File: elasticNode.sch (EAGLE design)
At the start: 101 parts, among them J1 ISP_CONN_6PIN, J2 FEMALE_HEADER_2X2, J3 FEMALE_HEADER_2X1, J4 FEMALE_HEADER_2X1, J5 FEMALE_HEADER_5X2, J6 FEMALE_HEADER_5X2, J7 JTAG_CONN_6PINTHT, J8 USB_CONNSMT, U1 ATMEGA64AQFN, U10 LTC3419DFN, U2 SST26VF032B, U3 MRF24J40MA, U4 SPARTAN6-LX9, U5 SST26VF032B, U6 PAC1720, U7 PAC1720, U8 PAC1720, U9 FT232RSSOP28, X1 12MHz, X2 50MHz, X3 32MHz

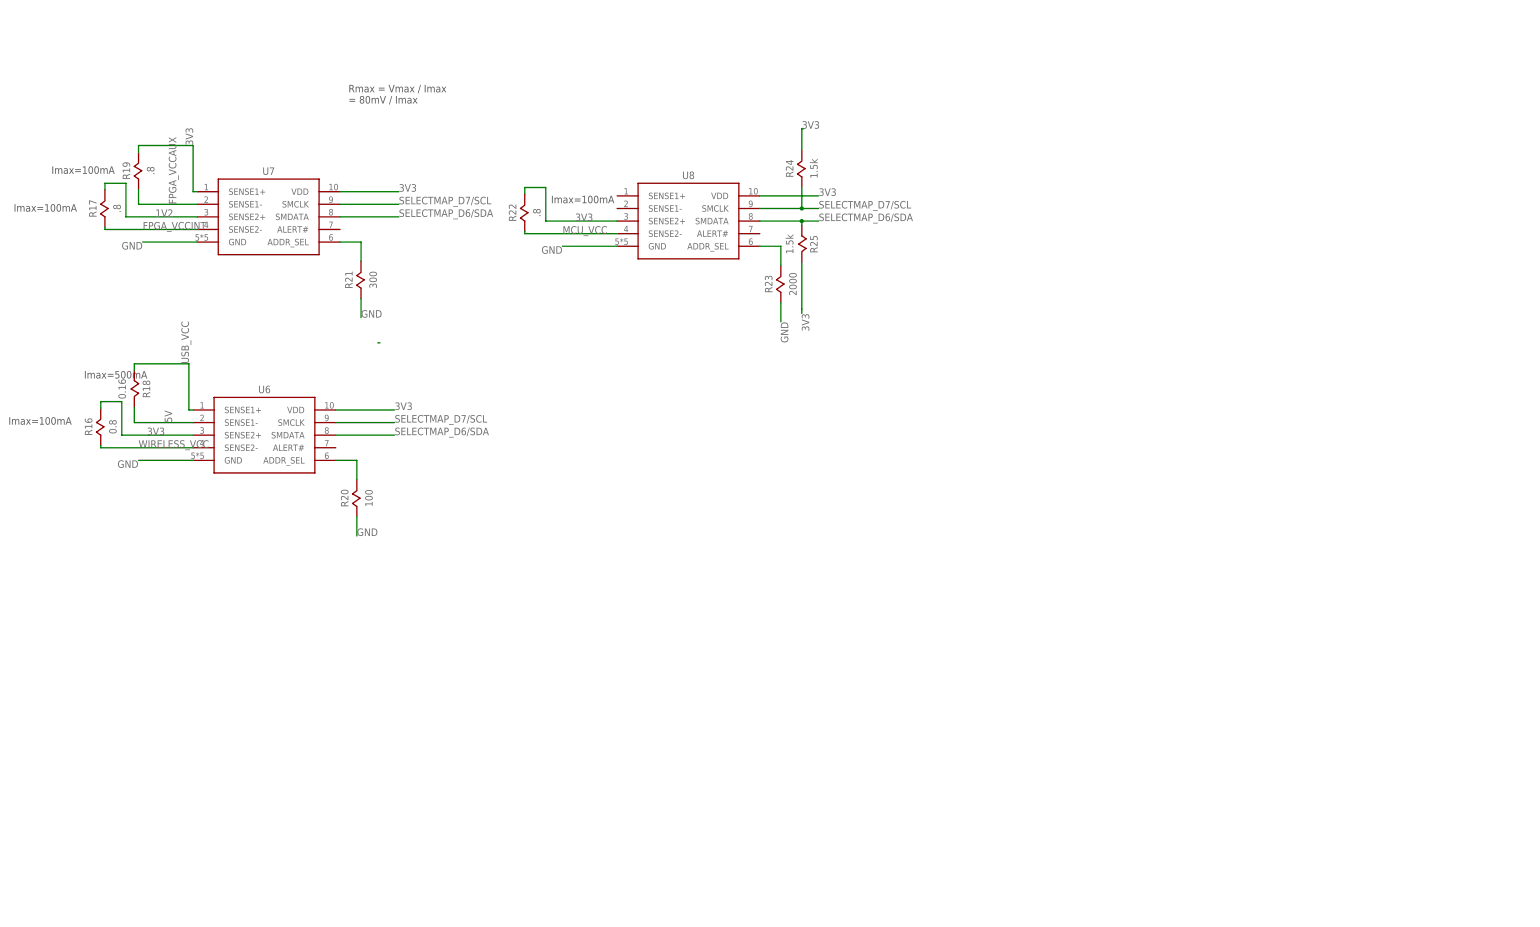
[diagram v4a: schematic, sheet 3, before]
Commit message: first part toward separate monitoring board
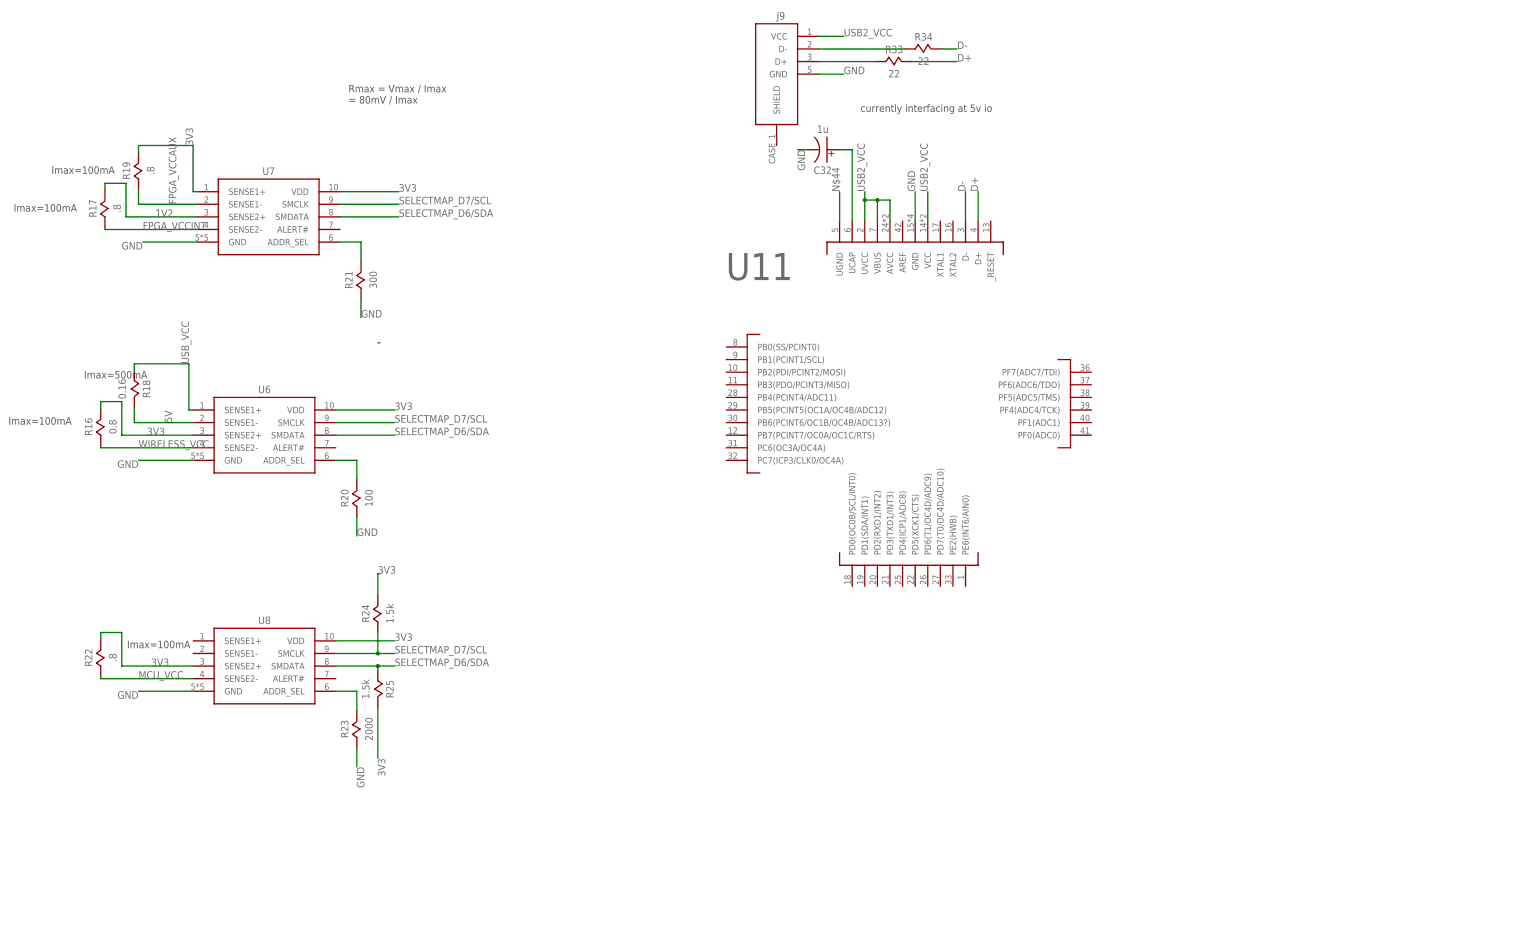
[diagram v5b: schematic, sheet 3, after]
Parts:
- added C32: 1u, passive:CAPACITOR0805
- added J9: USB_CONNSMT, connectors:USB_CONNSMT
- added R33, R34: 22, passive:RESISTOR
- added U11: ATMEGA32U4, ic:ATMEGA32U4
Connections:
- new net D+: R33.2, U11.D+
- new net D-: R34.2, U11.D-
- new net N$38: J9.D+, R33.1
- new net N$39: J9.D-, R34.1
- new net N$43: C32.P$1, U11.UCAP
- new net N$44: U11.UGND
- new net USB2_VCC: J9.VCC, U11.AVCC, U11.UVCC, U11.VBUS, U11.VCC
- net GND: now also C32.P$2, J9.GND, U11.GND
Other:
- note added: "currently interfacing at 5v io"
- moved on the sheet: R22, R23, R24, R25, U8

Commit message: first part of new layout
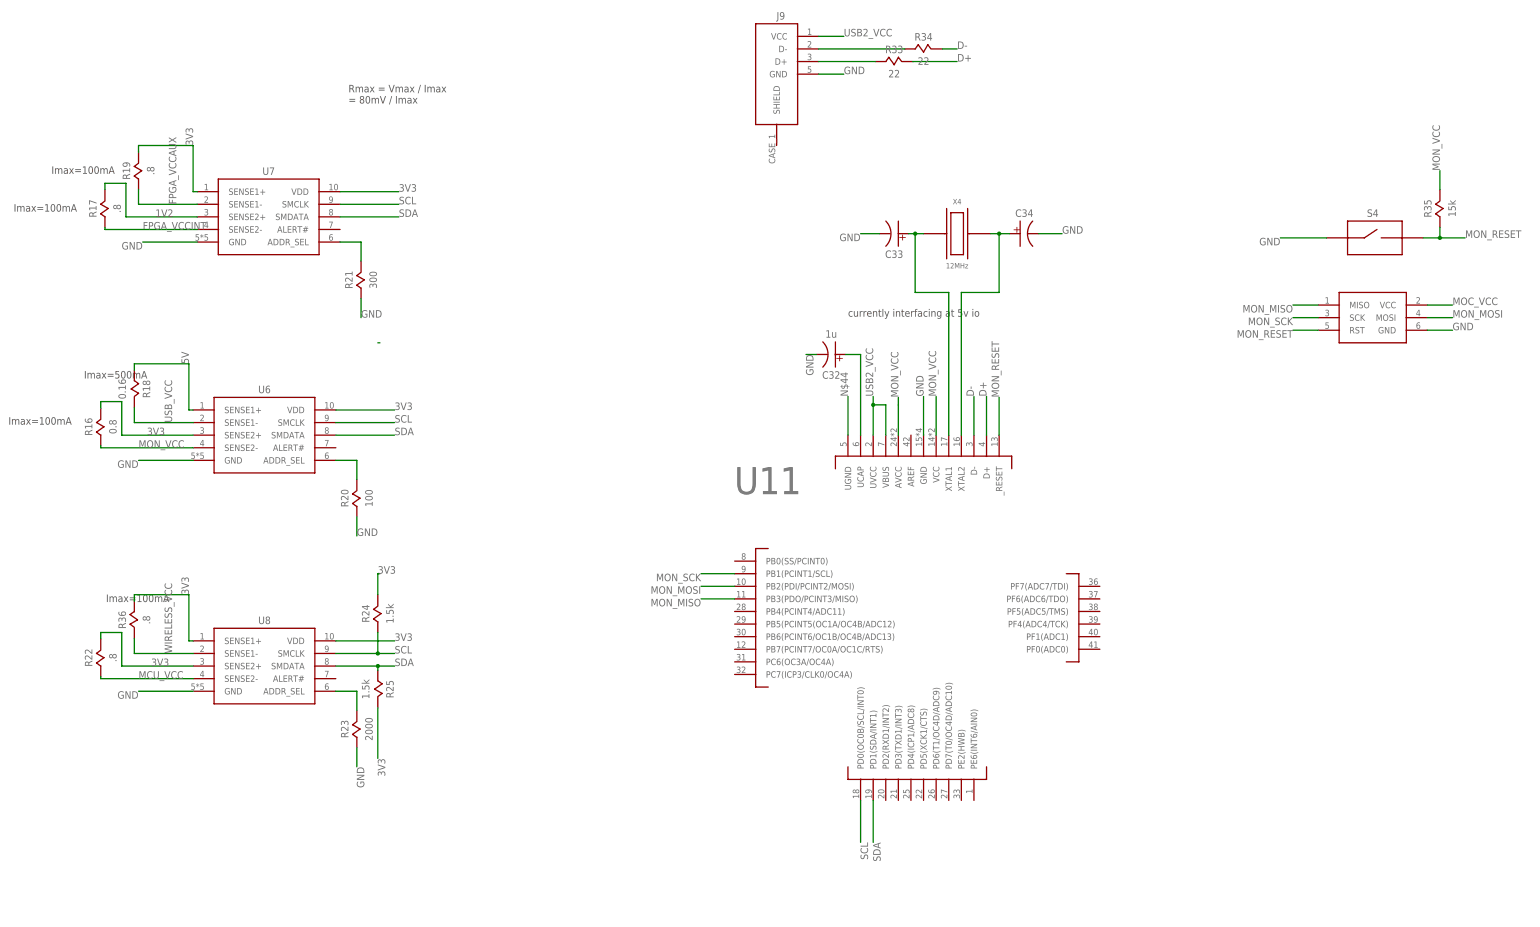
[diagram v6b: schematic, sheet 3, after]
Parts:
- removed J6: FEMALE_HEADER_5X2, connectors:FEMALE_HEADER_5X2
- removed J7: JTAG_CONN_6PINTHT, connectors:JTAG_CONN_6PINTHT
- added C33, C34: (no value), passive:CAPACITOR0805
- added C35, C36: 20p, passive:CAPACITOR0805
- added J10: ISP_CONN_6PIN, connectors:ISP_CONN_6PIN
- added R35: 15k, passive:RESISTOR
- added R36: .8, passive:RESISTOR
- added S4: SPST_BUTTON2PIN_SMT, connectors:SPST_BUTTON2PIN_SMT
- added X4: 12MHz, passive:QUARTZ
- J1: SPICEPREFIX (none) -> X
- J5: value FEMALE_HEADER_5X2 -> FEMALE_HEADER_10X2; device connectors:FEMALE_HEADER_5X2 -> connectors:FEMALE_HEADER_10X2
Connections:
- net N$43 renamed UCAP
- removed net AD0: U1.PA0_AD0, U4.IO_L1P_1
- removed net AD1: U1.PA1_AD1, U4.IO_L1N_VREF_1
- removed net AD2: U1.PA2_AD2, U4.IO_L32P_1
- removed net AD3: U1.PA3_AD3, U4.IO_L32N_1
- removed net AD4: U1.PA4_AD4, U4.IO_L33P_1
- removed net AD5: U1.PA5_AD5, U4.IO_L33N_1
- removed net AD6: U1.PA6_AD6, U4.IO_L34P_1
- removed net AD7: U1.PA7_AD7, U4.IO_L34N_1
- removed net SELECTMAP_D0/FPGA_MISO1: U1.PD7_T2, U4.IO_L3P_D0_DIN_MISO_MISO1_2, U5.SO
- removed net SELECTMAP_D1/FPGA_MISO2: U1.PD6_T1, U4.IO_L12P_D1_MISO2_2, U5.WP
- removed net SELECTMAP_D2/FPGA_MISO3: U1.PD5_XCK1, U4.IO_L12N_D2_MISO3_2, U5.HOLD
- removed net SELECTMAP_D3: U1.PD4_ICP1, U4.IO_L49P_D3_2
- removed net SELECTMAP_D4/MCU_TX1: U1.PD3_TXD1/INT3, U4.IO_L49N_D4_2
- removed net SELECTMAP_D5/MCU_RX1: U1.PD2_RXD1/INT2, U4.IO_L62P_D5_2
- removed net SELECTMAP_D6/SDA: R25.1, U1.PD1_SDA/INT1, U4.IO_L62N_D6_2, U6.SMDATA, U7.SMDATA, U8.SMDATA
- removed net SELECTMAP_D7/SCL: R24.1, U1.PD0_SCL/INT0, U4.IO_L48P_D7_2, U6.SMCLK, U7.SMCLK, U8.SMCLK
- new net AD0/SELECTMAP_D7: U1.PA0_AD0, U4.IO_L48P_D7_2
- new net AD1/SELECTMAP_D6: U1.PA1_AD1, U4.IO_L62N_D6_2
- new net AD2/SELECTMAP_D5/MCU_RX1: U1.PA2_AD2, U4.IO_L62P_D5_2
- new net AD3/SELECTMAP_D4/MCU_TX1: U1.PA3_AD3, U4.IO_L49N_D4_2
- new net AD4/SELECTMAP_D3: U1.PA4_AD4, U4.IO_L49P_D3_2
- new net AD5/SELECTMAP_D2/FPGA_MISO3: U1.PA5_AD5, U4.IO_L12N_D2_MISO3_2, U5.HOLD
- new net AD6/SELECTMAP_D1/FPGA_MISO2: U1.PA6_AD6, U4.IO_L12P_D1_MISO2_2, U5.WP
- new net AD7/SELECTMAP_D0/FPGA_MISO1: U1.PA7_AD7, U4.IO_L3P_D0_DIN_MISO_MISO1_2, U5.SO
- new net MCU_RX1: U1.PD2_RXD1/INT2, U9.TXD
- new net MCU_TX1: U1.PD3_TXD1/INT3, U9.RXD
- new net MOC_VCC: J10.VCC
- new net MON_MISO: J10.MISO, U11.PB3(PDO/PCINT3/MISO)
- new net MON_MOSI: J10.MOSI, U11.PB2(PDI/PCINT2/MOSI)
- new net MON_RESET: J10.RST, R35.1, S4.3, U11._RESET
- new net MON_SCK: J10.SCK, U11.PB1(PCINT1/SCL)
- new net MON_VCC: R16.1, R35.2, U11.AVCC, U11.VCC, U6.SENSE2-
- new net MON_XTAL1: C33.P$1, U11.XTAL1, X4.P$1
- new net MON_XTAL2: C34.P$1, U11.XTAL2, X4.P$2
- new net N$33: U1.PB5_OC1A
- new net N$46: U4.IO_L30N_GCLK0_USERCCLK_2
- new net SCL: R24.1, U11.PD0(OC0B/SCL/INT0), U6.SMCLK, U7.SMCLK, U8.SMCLK
- new net SDA: R25.1, U11.PD1(SDA/INT1), U6.SMDATA, U7.SMDATA, U8.SMDATA
- net 3V3: now also R36.1, U8.SENSE1+; no longer J7.REF
- net 5V: now also R18.1, U6.SENSE1+; no longer R18.2, U6.SENSE1-
- net A10: now also U4.IO_L46P_1; no longer U4.IO_L46N_1
- net A11: now also U4.IO_L46N_1; no longer U4.IO_L46P_1
- net A12: now also U4.IO_L47P_1; no longer U4.IO_L45N_1
- net A13: now also U4.IO_L47N_1; no longer U4.IO_L45P_1
- net A14: now also U4.IO_L74P_AWAKE_1; no longer U4.IO_L43N_GCLK4_1
- net A15: now also U4.IO_L74N_DOUT_BUSY_1; no longer U4.IO_L43P_GCLK5_1
- net A8: now also U4.IO_L45P_1; no longer U4.IO_L47N_1
- net A9: now also U4.IO_L45N_1; no longer U4.IO_L47P_1
- net ALE: now also U4.IO_L2N_CMPMOSI_2; no longer U4.IO_L40P_GCLK11_1
- net CCLK: now also U1.PD1_SDA/INT1; no longer U1.PG4_TOSC2
- net CSI_B/FPGA_MISO0: now also U1.PD0_SCL/INT0; no longer U1.PG3_TOSC2
- net FPGA_GPIO_0: now also J5.1; no longer J5.10
- net FPGA_GPIO_1: now also J5.20; no longer J5.1
- net FPGA_GPIO_10: now also J5.15, U4.IO_L44P_GCLK21_3; no longer J6.5, U4.IO_L41P_GCLK27_3
- net FPGA_GPIO_11: now also J5.6, U4.IO_L44N_GCLK20_3; no longer J6.6, U4.IO_L41N_GCLK26_3
- net FPGA_GPIO_12: now also J5.14, U4.IO_L43P_GCLK23_3; no longer J6.4, U4.IO_L37P_3
- net FPGA_GPIO_13: now also J5.7, U4.IO_L43N_GCLK22_IRDY2_3; no longer J6.7, U4.IO_L37N_3
- net FPGA_GPIO_14: now also J5.8, U4.IO_L42N_GCLK24_3; no longer J6.3, U4.IO_L36P_3
- net FPGA_GPIO_15: now also J5.13, U4.IO_L42P_GCLK25_TRDY2_3; no longer J6.8, U4.IO_L36N_3
- net FPGA_GPIO_16: now also J5.9, U4.IO_L41N_GCLK26_3; no longer J6.2, U4.IO_L2P_3
- net FPGA_GPIO_17: now also J5.12, U4.IO_L41P_GCLK27_3; no longer J6.9, U4.IO_L2N_3
- net FPGA_GPIO_18: now also J5.10, U4.IO_L37P_3; no longer J6.1, U4.IO_L1P_3
- net FPGA_GPIO_19: now also J5.11, U4.IO_L37N_3; no longer J6.10, U4.IO_L1N_VREF_3
- net FPGA_GPIO_2: now also J5.2; no longer J5.9
- net FPGA_GPIO_3: now also J5.19; no longer J5.2
- net FPGA_GPIO_4: now also J5.3; no longer J5.8
- net FPGA_GPIO_5: now also J5.18; no longer J5.3
- net FPGA_GPIO_6: now also J5.4; no longer J5.7
- net FPGA_GPIO_7: now also J5.17; no longer J5.4
- net FPGA_GPIO_8: now also J5.5; no longer J5.6
- net FPGA_GPIO_9: now also J5.16; no longer J5.5
- net FPGA_LED0: now also U4.IO_L1P_1; no longer U4.IO_L1P_HSWAPEN_0
- net FPGA_LED1: now also U4.IO_L1N_VREF_1; no longer U4.IO_L1N_VREF_0
- net FPGA_LED2: now also U4.IO_L32P_1; no longer U4.IO_L2P_0
- net FPGA_LED3: now also U4.IO_L32N_1; no longer U4.IO_L2N_0
- net FPGA_RESET: now also U1.PF2_ADC2; no longer U1.PB6_OC1B
- net FPGA_VCCAUX: now also C4.P$1; no longer C4.P$2
- net GND: now also C33.P$2, C34.P$2, C35.P$2, C36.P$2, C4.P$2, J10.GND, S4.1; no longer C4.P$1, J7.GND
- net INIT_B: now also U1.PF3_ADC3; no longer U1.PB7_OC2/OC1C
- net JTAG_TCK: no longer J7.TCK
- net JTAG_TDI: no longer J7.TDI
- net JTAG_TDO: no longer J7.TDO
- net JTAG_TMS: no longer J7.TMS
- net MCU_GPIO_0: now also U1.PB6_OC1B; no longer U1.PF3_ADC3
- net MCU_GPIO_1: now also U1.PE4_OC3B/INT4; no longer U1.PF2_ADC2
- net MCU_GPIO_2: now also U1.PB7_OC2/OC1C; no longer U1.PF1_ADC1
- net MCU_LED0: now also U1.PD7_T2; no longer U1.PB5_OC1A
- net MCU_LED1: now also U1.PD6_T1
- net MCU_LED2: now also U1.PD5_XCK1
- net MCU_LED3: now also U1.PD4_ICP1
- net MCU_RX0/PDI: no longer U9.TXD
- net MCU_TX0/PDO: no longer U9.RXD
- net RD: now also U4.IO_L43N_GCLK4_1; no longer U4.IO_L74P_AWAKE_1
- net USB2_VCC: no longer U11.AVCC, U11.VCC
- net USB_VCC: now also R18.2, U6.SENSE1-; no longer R18.1, U6.SENSE1+
- net WIRELESS_CS: now also U1.PF1_ADC1; no longer U1.PE4_OC3B/INT4
- net WIRELESS_VCC: now also R36.2, U8.SENSE1-; no longer R16.1, U6.SENSE2-
- net WR: now also U4.IO_L43P_GCLK5_1; no longer U4.IO_L74N_DOUT_BUSY_1
- net XTAL1: now also C36.P$1, X1.P$1; no longer X1.P$2
- net XTAL2: now also C35.P$1, X1.P$2; no longer X1.P$1
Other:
- moved on the sheet: C32, C4, U11, X1
